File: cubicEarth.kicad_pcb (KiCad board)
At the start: 2 copper layers, 32 x 35 mm, 33 parts, among them J1 TYPE-C-31-M-12, J2 LCD, Q1 NPN, Q2 NPN, SW1 TS24ZJ, U1 CP2102N-A02-GQFN24R, U2 AW9364DNR, U3 AMS1117-3.3, U4 ESP32-PICO-V3-02

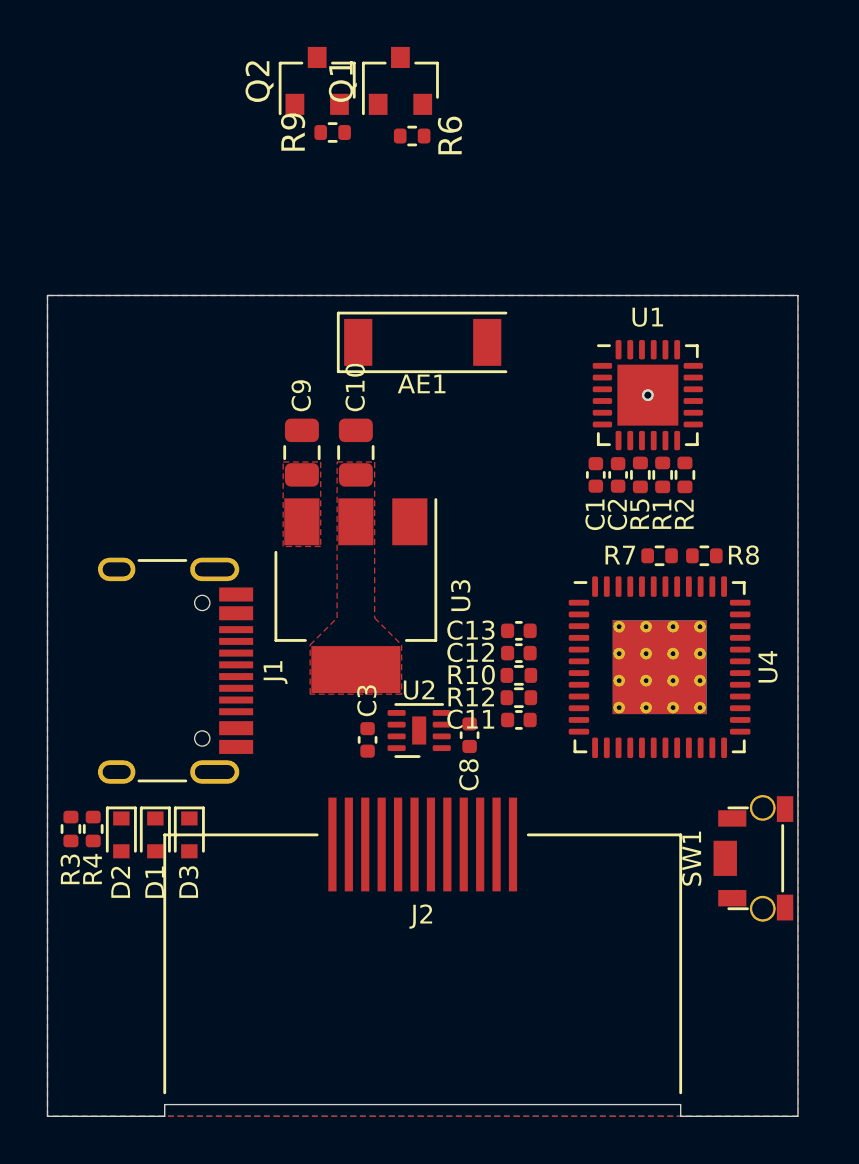
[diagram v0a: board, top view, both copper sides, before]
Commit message: Use an SOT-563 dual NPN instead of 2 separated NPN
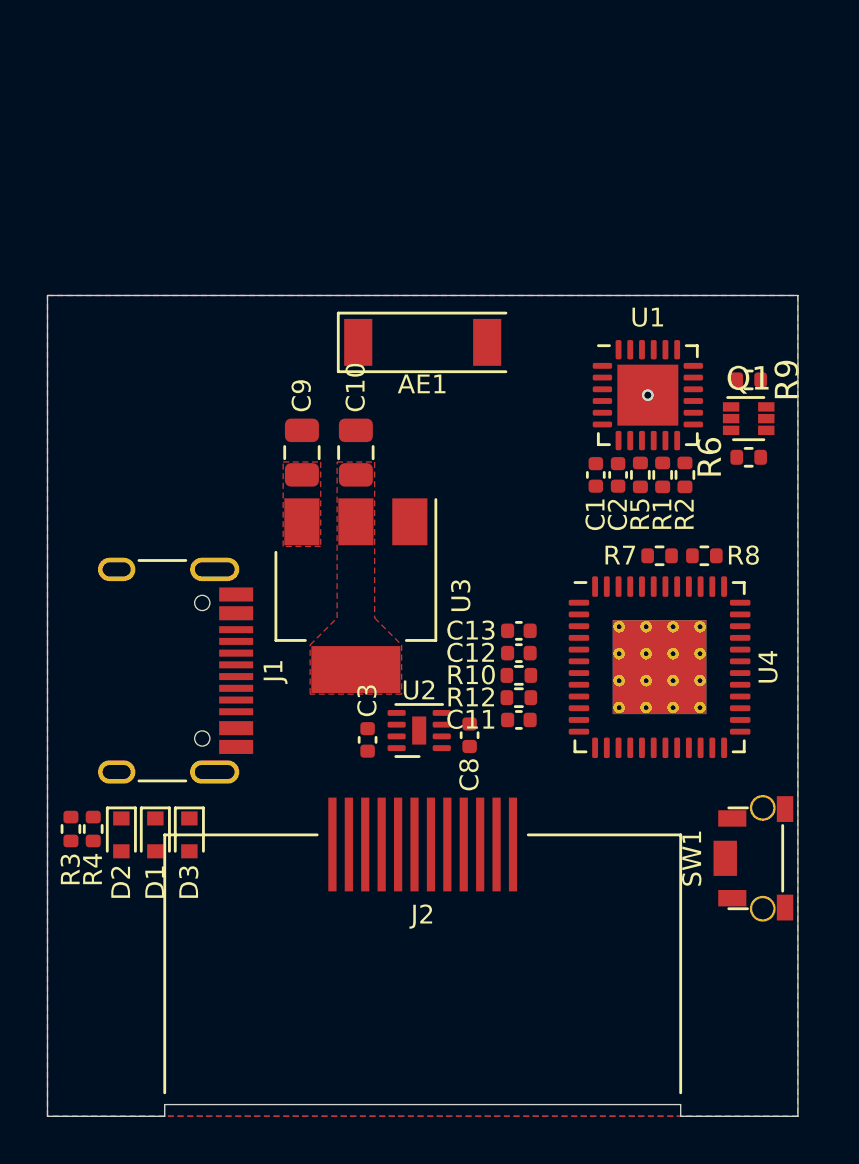
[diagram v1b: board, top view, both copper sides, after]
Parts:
- removed Q2: NPN, Package_TO_SOT_SMD:SOT-23
- Q1: value NPN -> BC847BVC-7; footprint Package_TO_SOT_SMD:SOT-23 -> Package_TO_SOT_SMD:SOT-563
- moved Q1 20.7 mm to (113.9, 89.2), turned to 0 degrees
- moved R9 20.6 mm to (113.9, 87.6), turned to 180 degrees
- moved R6 19.8 mm to (113.9, 90.9), turned to 180 degrees
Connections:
- Q1 pad 3: /BOOT -> /EN
- R6 pad 1: Net-(Q1-Pad1) -> Net-(Q1-Pad2)
- R9 pad 2: Net-(Q1-Pad2) -> Net-(Q1-Pad1)

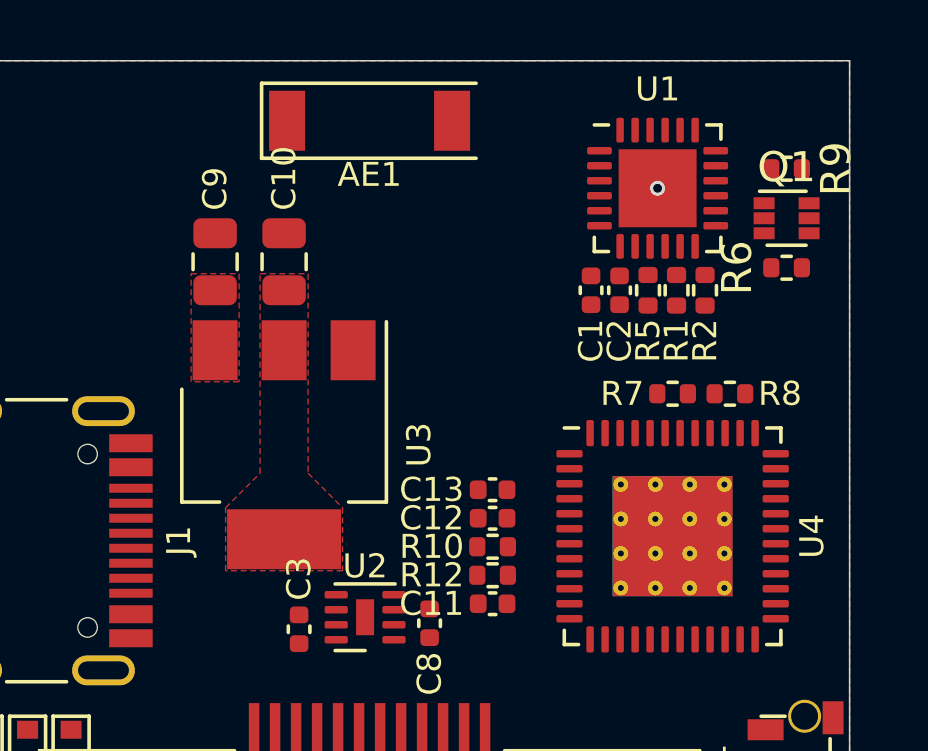
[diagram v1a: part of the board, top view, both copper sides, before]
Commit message: Use LP2992AIM5X-3.3 instead of AMS1117-3.3
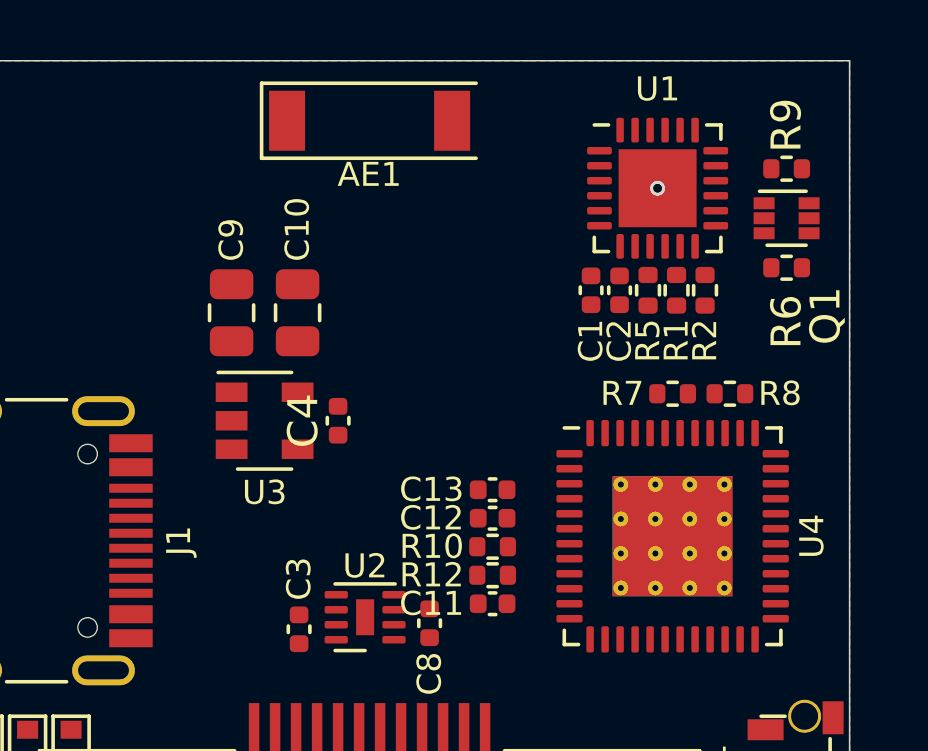
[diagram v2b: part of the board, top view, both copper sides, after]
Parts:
- added C4: 10nF, Capacitor_SMD:C_0402_1005Metric, F.Cu at (99.0, 96.0)
- U3: value AMS1117-3.3 -> LP2992AIM5X-3.3; footprint Package_TO_SOT_SMD:SOT-223-3_TabPin2 -> Package_TO_SOT_SMD:SOT-23-5
- moved C9 1.79 mm to (95.4, 92.4)
- moved C10 1.76 mm to (97.6, 92.4)
- moved U3 1.03 mm to (96.5, 96.0), turned to 0 degrees
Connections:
- U3 pad 1: GND -> +5V
- U3 pad 2: +3V3 -> GND
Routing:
- removed copper zone on F.Cu, net +3V3
- removed copper zone on F.Cu, net +5V
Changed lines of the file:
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@@
     (tracks 1)
     (zones 0)
-    (modules 32)
-    (nets 29)
+    (modules 33)
+    (nets 30)
   )
   (page A4)
@@
   (net 27 /USB_TX)
   (net 28 /DTR)
+  (net 29 "Net-(C4-Pad1)")
   (net_class Default "This is the default net class."
     (clearance 0.15)
@@
     (add_net GND)
     (add_net "Net-(AE1-Pad1)")
+    (add_net "Net-(C4-Pad1)")
     (add_net "Net-(J1-PadA5)")
     (add_net "Net-(J1-PadA8)")
@@
     (add_net "Net-(Q1-Pad1)")
     (add_net "Net-(Q1-Pad2)")
-    (add_net "Net-(Q3-Pad1)")
-    (add_net "Net-(Q3-Pad2)")
-    (add_net "Net-(Q3-Pad3)")
-    (add_net "Net-(Q3-Pad4)")
-    (add_net "Net-(Q3-Pad5)")
-    (add_net "Net-(Q3-Pad6)")
     (add_net "Net-(R1-Pad1)")
     (add_net "Net-(R5-Pad1)")
@@
     (diff_pair_gap 0.15)
   )
+  (module Package_TO_SOT_SMD:SOT-23-5 (layer F.Cu)
+    (at 96.5 96)
+    (descr "5-pin SOT23 package")
+    (tags SOT-23-5)
+    (attr smd)
+    (fp_text reference U3 (at 0 2.4) (layer F.SilkS)
+      (effects (font (size 0.8 0.8) (thickness 0.12)))
+    )
+    (fp_text value LP2992AIM5X-3.3 (at 0 2.9) (layer F.Fab)
+      (effects (font (size 1 1) (thickness 0.15)))
+    )
+    (fp_text user %R (at 0 0 90) (layer F.Fab)
+      (effects (font (size 0.5 0.5) (thickness 0.075)))
+    )
+    (fp_line (start -0.9 1.61) (end 0.9 1.61) (layer F.SilkS) (width 0.12))
+    (fp_line (start 0.9 -1.61) (end -1.55 -1.61) (layer F.SilkS) (width 0.12))
+    (fp_line (start -1.9 -1.8) (end 1.9 -1.8) (layer F.CrtYd) (width 0.05))
+    (fp_line (start 1.9 -1.8) (end 1.9 1.8) (layer F.CrtYd) (width 0.05))
+    (fp_line (start 1.9 1.8) (end -1.9 1.8) (layer F.CrtYd) (width 0.05))
+    (fp_line (start -1.9 1.8) (end -1.9 -1.8) (layer F.CrtYd) (width 0.05))
+    (fp_line (start -0.9 -0.9) (end -0.25 -1.55) (layer F.Fab) (width 0.1))
+    (fp_line (start 0.9 -1.55) (end -0.25 -1.55) (layer F.Fab) (width 0.1))
+    (fp_line (start -0.9 -0.9) (end -0.9 1.55) (layer F.Fab) (width 0.1))
+    (fp_line (start 0.9 1.55) (end -0.9 1.55) (layer F.Fab) (width 0.1))
+    (fp_line (start 0.9 -1.55) (end 0.9 1.55) (layer F.Fab) (width 0.1))
+    (pad 5 smd rect (at 1.1 -0.95) (size 1.06 0.65) (layers F.Cu F.Paste F.Mask)
+      (net 5 +3V3))
+    (pad 4 smd rect (at 1.1 0.95) (size 1.06 0.65) (layers F.Cu F.Paste F.Mask)
+      (net 29 "Net-(C4-Pad1)"))
+    (pad 3 smd rect (at -1.1 0.95) (size 1.06 0.65) (layers F.Cu F.Paste F.Mask)
+      (net 4 +5V))
+    (pad 2 smd rect (at -1.1 0) (size 1.06 0.65) (layers F.Cu F.Paste F.Mask)
+      (net 1 GND))
+    (pad 1 smd rect (at -1.1 -0.95) (size 1.06 0.65) (layers F.Cu F.Paste F.Mask)
+      (net 4 +5V))
+    (model ${KISYS3DMOD}/Package_TO_SOT_SMD.3dshapes/SOT-23-5.wrl
+      (at (xyz 0 0 0))
+      (scale (xyz 1 1 1))
+      (rotate (xyz 0 0 0))
+    )
+  )
+  (module Capacitor_SMD:C_0402_1005Metric (layer F.Cu)
+    (at 98.95 96 90)
+    (descr "Capacitor SMD 0402 (1005 Metric), square (rectangular) end terminal, IPC_7351 nominal, (Body size source: IPC-SM-782 page 76, https://www.pcb-3d.com/wordpress/wp-content/uploads/ipc-sm-782a_amendment_1_and_2.pdf), generated with kicad-footprint-generator")
+    (tags capacitor)
+    (attr smd)
+    (fp_text reference C4 (at 0 -1.16 90) (layer F.SilkS)
+      (effects (font (size 1 1) (thickness 0.15)))
+    )
+    (fp_text value 10nF (at 0 1.16 90) (layer F.Fab)
+      (effects (font (size 1 1) (thickness 0.15)))
+    )
+    (fp_text user %R (at 0 0 90) (layer F.Fab)
+      (effects (font (size 0.25 0.25) (thickness 0.04)))
+    )
+    (fp_line (start -0.5 0.25) (end -0.5 -0.25) (layer F.Fab) (width 0.1))
+    (fp_line (start -0.5 -0.25) (end 0.5 -0.25) (layer F.Fab) (width 0.1))
+    (fp_line (start 0.5 -0.25) (end 0.5 0.25) (layer F.Fab) (width 0.1))
+    (fp_line (start 0.5 0.25) (end -0.5 0.25) (layer F.Fab) (width 0.1))
+    (fp_line (start -0.107836 -0.36) (end 0.107836 -0.36) (layer F.SilkS) (width 0.12))
+    (fp_line (start -0.107836 0.36) (end 0.107836 0.36) (layer F.SilkS) (width 0.12))
+    (fp_line (start -0.91 0.46) (end -0.91 -0.46) (layer F.CrtYd) (width 0.05))
+    (fp_line (start -0.91 -0.46) (end 0.91 -0.46) (layer F.CrtYd) (width 0.05))
+    (fp_line (start 0.91 -0.46) (end 0.91 0.46) (layer F.CrtYd) (width 0.05))
+    (fp_line (start 0.91 0.46) (end -0.91 0.46) (layer F.CrtYd) (width 0.05))
+    (pad 2 smd roundrect (at 0.48 0 90) (size 0.56 0.62) (layers F.Cu F.Paste F.Mask) (roundrect_rratio 0.25)
+      (net 1 GND))
+    (pad 1 smd roundrect (at -0.48 0 90) (size 0.56 0.62) (layers F.Cu F.Paste F.Mask) (roundrect_rratio 0.25)
+      (net 29 "Net-(C4-Pad1)"))
+    (model ${KISYS3DMOD}/Capacitor_SMD.3dshapes/C_0402_1005Metric.wrl
+      (at (xyz 0 0 0))
+      (scale (xyz 1 1 1))
+      (rotate (xyz 0 0 0))
+    )
+  )
   (module Package_TO_SOT_SMD:SOT-563 (layer F.Cu)
     (at 113.9 89.25)
@@
     (tags SOT-563)
     (attr smd)
-    (fp_text reference Q1 (at 0 -1.7) (layer F.SilkS)
+    (fp_text reference Q1 (at 1.3 3.25 90) (layer F.SilkS)
       (effects (font (size 1 1) (thickness 0.15)))
     )
@@
     (tags resistor)
     (attr smd)
-    (fp_text reference R9 (at -1.65 0 90) (layer F.SilkS)
+    (fp_text reference R9 (at 0 1.45 90) (layer F.SilkS)
       (effects (font (size 1 1) (thickness 0.15)))
     )
@@
     (tags resistor)
     (attr smd)
-    (fp_text reference R6 (at 1.65 0 270) (layer F.SilkS)
+    (fp_text reference R6 (at 0 -1.8 270) (layer F.SilkS)
       (effects (font (size 1 1) (thickness 0.15)))
     )
@@
   )
   (module Capacitor_SMD:C_0805_2012Metric (layer F.Cu)
-    (at 97.15 90.700001 90)
+    (at 97.6 92.4 90)
     (descr "Capacitor SMD 0805 (2012 Metric), square (rectangular) end terminal, IPC_7351 nominal, (Body size source: IPC-SM-782 page 76, https://www.pcb-3d.com/wordpress/wp-content/uploads/ipc-sm-782a_amendment_1_and_2.pdf, https://docs.google.com/spreadsheets/d/1BsfQQcO9C6DZCsRaXUlFlo91Tg2WpOkGARC1WS5S8t0/edit?usp=sharing), generated with kicad-footprint-generator")
     (tags capacitor)
@@
   )
   (module Capacitor_SMD:C_0805_2012Metric (layer F.Cu)
-    (at 94.85 90.699998 90)
+    (at 95.4 92.4 90)
     (descr "Capacitor SMD 0805 (2012 Metric), square (rectangular) end terminal, IPC_7351 nominal, (Body size source: IPC-SM-782 page 76, https://www.pcb-3d.com/wordpress/wp-content/uploads/ipc-sm-782a_amendment_1_and_2.pdf, https://docs.google.com/spreadsheets/d/1BsfQQcO9C6DZCsRaXUlFlo91Tg2WpOkGARC1WS5S8t0/edit?usp=sharing), generated with kicad-footprint-generator")
     (tags capacitor)
@@
     )
   )
-  (module Package_TO_SOT_SMD:SOT-223-3_TabPin2 (layer F.Cu)
-    (at 97.15 96.8 270)
-    (descr "module CMS SOT223 4 pins")
-    (tags "CMS SOT")
-    (attr smd)
-    (fp_text reference U3 (at 0 -4.5 90) (layer F.SilkS)
-      (effects (font (size 0.8 0.8) (thickness 0.12)))
-    )
-    (fp_text value AMS1117-3.3 (at 0 4.5 90) (layer F.Fab)
-      (effects (font (size 1 1) (thickness 0.15)))
-    )
-    (fp_line (start 1.85 -3.35) (end 1.85 3.35) (layer F.Fab) (width 0.1))
-    (fp_line (start -1.85 3.35) (end 1.85 3.35) (layer F.Fab) (width 0.1))
-    (fp_line (start -4.1 -3.41) (end 1.91 -3.41) (layer F.SilkS) (width 0.12))
-    (fp_line (start -0.85 -3.35) (end 1.85 -3.35) (layer F.Fab) (width 0.1))
-    (fp_line (start -1.85 3.41) (end 1.91 3.41) (layer F.SilkS) (width 0.12))
-    (fp_line (start -1.85 -2.35) (end -1.85 3.35) (layer F.Fab) (width 0.1))
-    (fp_line (start -1.85 -2.35) (end -0.85 -3.35) (layer F.Fab) (width 0.1))
-    (fp_line (start -4.4 -3.6) (end -4.4 3.6) (layer F.CrtYd) (width 0.05))
-    (fp_line (start -4.4 3.6) (end 4.4 3.6) (layer F.CrtYd) (width 0.05))
-    (fp_line (start 4.4 3.6) (end 4.4 -3.6) (layer F.CrtYd) (width 0.05))
-    (fp_line (start 4.4 -3.6) (end -4.4 -3.6) (layer F.CrtYd) (width 0.05))
-    (fp_line (start 1.91 -3.41) (end 1.91 -2.15) (layer F.SilkS) (width 0.12))
-    (fp_line (start 1.91 3.41) (end 1.91 2.15) (layer F.SilkS) (width 0.12))
-    (fp_text user %R (at 0 0) (layer F.Fab)
-      (effects (font (size 0.8 0.8) (thickness 0.12)))
-    )
-    (pad 1 smd rect (at -3.15 -2.3 270) (size 2 1.5) (layers F.Cu F.Paste F.Mask)
-      (net 1 GND))
-    (pad 3 smd rect (at -3.15 2.3 270) (size 2 1.5) (layers F.Cu F.Paste F.Mask)
-      (net 4 +5V))
-    (pad 2 smd rect (at -3.15 0 270) (size 2 1.5) (layers F.Cu F.Paste F.Mask)
-      (net 5 +3V3))
-    (pad 2 smd rect (at 3.15 0 270) (size 2 3.8) (layers F.Cu F.Paste F.Mask)
-      (net 5 +3V3))
-    (model ${KISYS3DMOD}/Package_TO_SOT_SMD.3dshapes/SOT-223.wrl
-      (at (xyz 0 0 0))
-      (scale (xyz 1 1 1))
-      (rotate (xyz 0 0 0))
-    )
-  )
   (module JLC-SMT:AW9364DNR_DFN2x2-8L (layer F.Cu)
     (at 99.85 102.55 180)
@@
       )
     )
-  )
-  (zone (net 5) (net_name +3V3) (layer F.Cu) (hatch full 0.508)
-    (priority 1)
-    (connect_pads yes (clearance 0.15))
-    (min_thickness 0.254)
-    (fill yes (arc_segments 32) (thermal_gap 0.15) (thermal_bridge_width 0.508) (smoothing fillet) (radius 0.1))
-    (polygon
-      (pts
-        (xy 95.2 101.000001) (xy 95.199999 98.900001) (xy 96.35 97.75) (xy 96.35 91.1) (xy 97.95 91.1)
-        (xy 97.95 97.75) (xy 99.1 98.900001) (xy 99.1 100.999999)
-      )
-    )
-  )
-  (zone (net 4) (net_name +5V) (layer F.Cu) (hatch full 0.508)
-    (priority 1)
-    (connect_pads yes (clearance 0.15))
-    (min_thickness 0.254)
-    (fill yes (arc_segments 32) (thermal_gap 0.15) (thermal_bridge_width 0.508) (smoothing fillet) (radius 1))
-    (polygon
-      (pts
-        (xy 94.05 94.7) (xy 94.050001 91.1) (xy 95.650001 91.100003) (xy 95.65 94.7)
-      )
-    )
